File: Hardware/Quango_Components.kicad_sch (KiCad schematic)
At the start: 112 parts, among them J1 Conn_01x12_Male, J2 Conn_01x12_Male, J3 Conn_01x12_Male, J4 Conn_01x12_Male, J5 SWD_Header, J6 Eurorack_10_pin_power, Q1 MMBT3904, U1 LM1117-3.3, U2 STM32G473V, U3 LM1117-5.0, U4 PS508, U5 MCP6002, U6 AS3364, U7 AS3364, U8 AD5676, U9 MCP48CMB21, Y1 8MHz 20pF

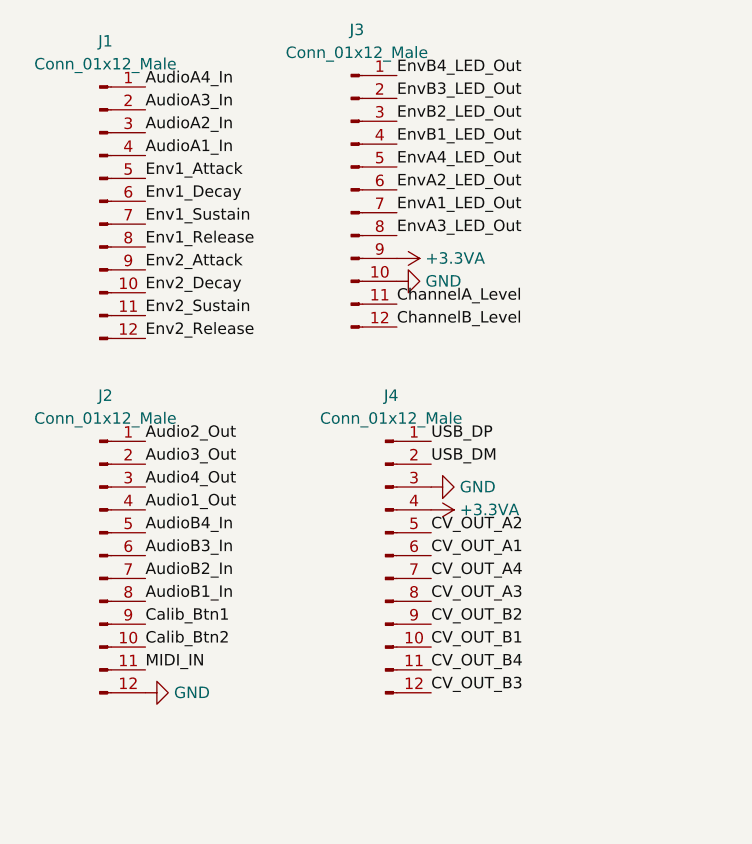
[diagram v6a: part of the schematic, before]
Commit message: Added individual audio channel breakout
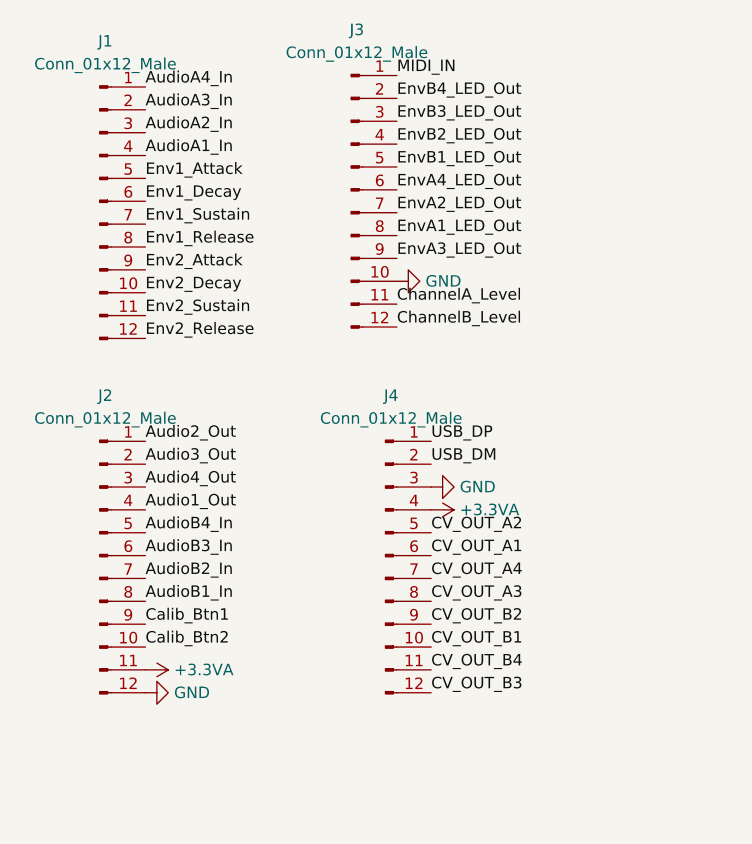
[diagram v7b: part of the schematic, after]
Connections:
- net +3.3VA: now also J2.11 (Pin_11); no longer J3.9 (Pin_9)
- net EnvA1_LED_Out: now also J3.8 (Pin_8); no longer J3.7 (Pin_7)
- net EnvA2_LED_Out: now also J3.7 (Pin_7); no longer J3.6 (Pin_6)
- net EnvA3_LED_Out: now also J3.9 (Pin_9); no longer J3.8 (Pin_8)
- net EnvA4_LED_Out: now also J3.6 (Pin_6); no longer J3.5 (Pin_5)
- net EnvB1_LED_Out: now also J3.5 (Pin_5); no longer J3.4 (Pin_4)
- net EnvB2_LED_Out: now also J3.4 (Pin_4); no longer J3.3 (Pin_3)
- net EnvB3_LED_Out: now also J3.3 (Pin_3); no longer J3.2 (Pin_2)
- net EnvB4_LED_Out: now also J3.2 (Pin_2); no longer J3.1 (Pin_1)
- net MIDI_IN: now also J3.1 (Pin_1); no longer J2.11 (Pin_11)
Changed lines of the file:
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@@
     (effects (font (size 1.27 1.27)) (justify left bottom))
   )
-  (label "EnvA3_LED_Out" (at -175.26 -66.04 0)
+  (label "EnvA3_LED_Out" (at -175.26 -63.5 0)
     (effects (font (size 1.27 1.27)) (justify left bottom))
   )
@@
     (effects (font (size 1.27 1.27)) (justify right bottom))
   )
-  (label "EnvB4_LED_Out" (at -175.26 -83.82 0)
+  (label "EnvB4_LED_Out" (at -175.26 -81.28 0)
     (effects (font (size 1.27 1.27)) (justify left bottom))
   )
@@
     (effects (font (size 1.27 1.27)) (justify left bottom))
   )
-  (label "EnvB2_LED_Out" (at -175.26 -78.74 0)
+  (label "EnvB2_LED_Out" (at -175.26 -76.2 0)
     (effects (font (size 1.27 1.27)) (justify left bottom))
   )
@@
     (effects (font (size 1.27 1.27)) (justify right bottom))
   )
-  (label "MIDI_IN" (at -203.2 -17.78 0)
+  (label "MIDI_IN" (at -175.26 -83.82 0)
     (effects (font (size 1.27 1.27)) (justify left bottom))
   )
@@
     (effects (font (size 1.27 1.27)) (justify left bottom))
   )
-  (label "EnvB3_LED_Out" (at -175.26 -81.28 0)
+  (label "EnvB3_LED_Out" (at -175.26 -78.74 0)
     (effects (font (size 1.27 1.27)) (justify left bottom))
   )
@@
     (effects (font (size 1.27 1.27)) (justify right bottom))
   )
-  (label "EnvA1_LED_Out" (at -175.26 -68.58 0)
+  (label "EnvA1_LED_Out" (at -175.26 -66.04 0)
     (effects (font (size 1.27 1.27)) (justify left bottom))
   )
@@
     (effects (font (size 1.27 1.27)) (justify right bottom))
   )
-  (label "EnvB1_LED_Out" (at -175.26 -76.2 0)
+  (label "EnvB1_LED_Out" (at -175.26 -73.66 0)
     (effects (font (size 1.27 1.27)) (justify left bottom))
   )
@@
     (effects (font (size 1.27 1.27)) (justify right bottom))
   )
-  (label "EnvA4_LED_Out" (at -175.26 -73.66 0)
+  (label "EnvA4_LED_Out" (at -175.26 -71.12 0)
     (effects (font (size 1.27 1.27)) (justify left bottom))
   )
@@
     (effects (font (size 1.27 1.27)) (justify left bottom))
   )
-  (label "EnvA2_LED_Out" (at -175.26 -71.12 0)
+  (label "EnvA2_LED_Out" (at -175.26 -68.58 0)
     (effects (font (size 1.27 1.27)) (justify left bottom))
   )
@@
     (pin "99")
   )
-  (symbol (lib_id "power:+3.3VA") (at -175.26 -63.5 270) (unit 1)
+  (symbol (lib_id "power:+3.3VA") (at -203.2 -17.78 270) (unit 1)
     (in_bom yes) (on_board yes) (fields_autoplaced)
-    (property "Reference" "#PWR02" (id 0) (at -179.07 -63.5 0)
+    (property "Reference" "#PWR02" (id 0) (at -207.01 -17.78 0)
       (effects (font (size 1.27 1.27)) hide)
     )
-    (property "Value" "+3.3VA" (id 1) (at -172.085 -63.5001 90)
+    (property "Value" "+3.3VA" (id 1) (at -200.025 -17.7801 90)
       (effects (font (size 1.27 1.27)) (justify left))
     )
-    (property "Footprint" "" (id 2) (at -175.26 -63.5 0)
+    (property "Footprint" "" (id 2) (at -203.2 -17.78 0)
       (effects (font (size 1.27 1.27)) hide)
     )
-    (property "Datasheet" "" (id 3) (at -175.26 -63.5 0)
+    (property "Datasheet" "" (id 3) (at -203.2 -17.78 0)
       (effects (font (size 1.27 1.27)) hide)
     )
@@
       (reference "J6") (unit 1) (value "Eurorack_10_pin_power") (footprint "Custom_Footprints:Eurorack_10_pin_header")
     )
+    (path "/6505d480-2c4a-43b6-864d-d09e21056980/2e1ddcad-0519-4706-9430-55bb3ce32171"
+      (reference "J7") (unit 1) (value "Audio_Breakout") (footprint "Connector_PinHeader_2.54mm:PinHeader_2x04_P2.54mm_Vertical")
+    )
     (path "/9cc3873a-349e-4fee-be4e-7429042177a8"
       (reference "L1") (unit 1) (value "L_Small") (footprint "Inductor_SMD:L_0805_2012Metric_Pad1.05x1.20mm_HandSolder")
@@
     )
     (path "/6505d480-2c4a-43b6-864d-d09e21056980/1b727df7-cb3f-48d1-be9c-292996b508c3"
-      (reference "U14") (unit 1) (value "TL074") (footprint "Package_SO:TSSOP-14_4.4x5mm_P0.65mm")
+      (reference "U14") (unit 1) (value "TL074") (footprint "Package_SO:SOIC-14_3.9x8.7mm_P1.27mm")
     )
     (path "/6505d480-2c4a-43b6-864d-d09e21056980/dfb0e318-b14d-499c-a2a3-d6ddf83ef63a"
-      (reference "U14") (unit 2) (value "TL074") (footprint "Package_SO:TSSOP-14_4.4x5mm_P0.65mm")
+      (reference "U14") (unit 2) (value "TL074") (footprint "Package_SO:SOIC-14_3.9x8.7mm_P1.27mm")
     )
     (path "/6505d480-2c4a-43b6-864d-d09e21056980/b690f45c-fd5f-4e22-a898-b1a3ca1d64ff"
-      (reference "U14") (unit 3) (value "TL074") (footprint "Package_SO:TSSOP-14_4.4x5mm_P0.65mm")
+      (reference "U14") (unit 3) (value "TL074") (footprint "Package_SO:SOIC-14_3.9x8.7mm_P1.27mm")
     )
     (path "/6505d480-2c4a-43b6-864d-d09e21056980/d7490e05-e2b4-473a-9389-d362b2a1506b"
-      (reference "U14") (unit 4) (value "TL074") (footprint "Package_SO:TSSOP-14_4.4x5mm_P0.65mm")
+      (reference "U14") (unit 4) (value "TL074") (footprint "Package_SO:SOIC-14_3.9x8.7mm_P1.27mm")
     )
     (path "/6505d480-2c4a-43b6-864d-d09e21056980/9b9b9766-bc41-4a1e-b4e6-58c18cc0519f"
-      (reference "U14") (unit 5) (value "TL074") (footprint "Package_SO:TSSOP-14_4.4x5mm_P0.65mm")
+      (reference "U14") (unit 5) (value "TL074") (footprint "Package_SO:SOIC-14_3.9x8.7mm_P1.27mm")
     )
     (path "/226694b0-ec80-4137-9308-0689e83ebb68"

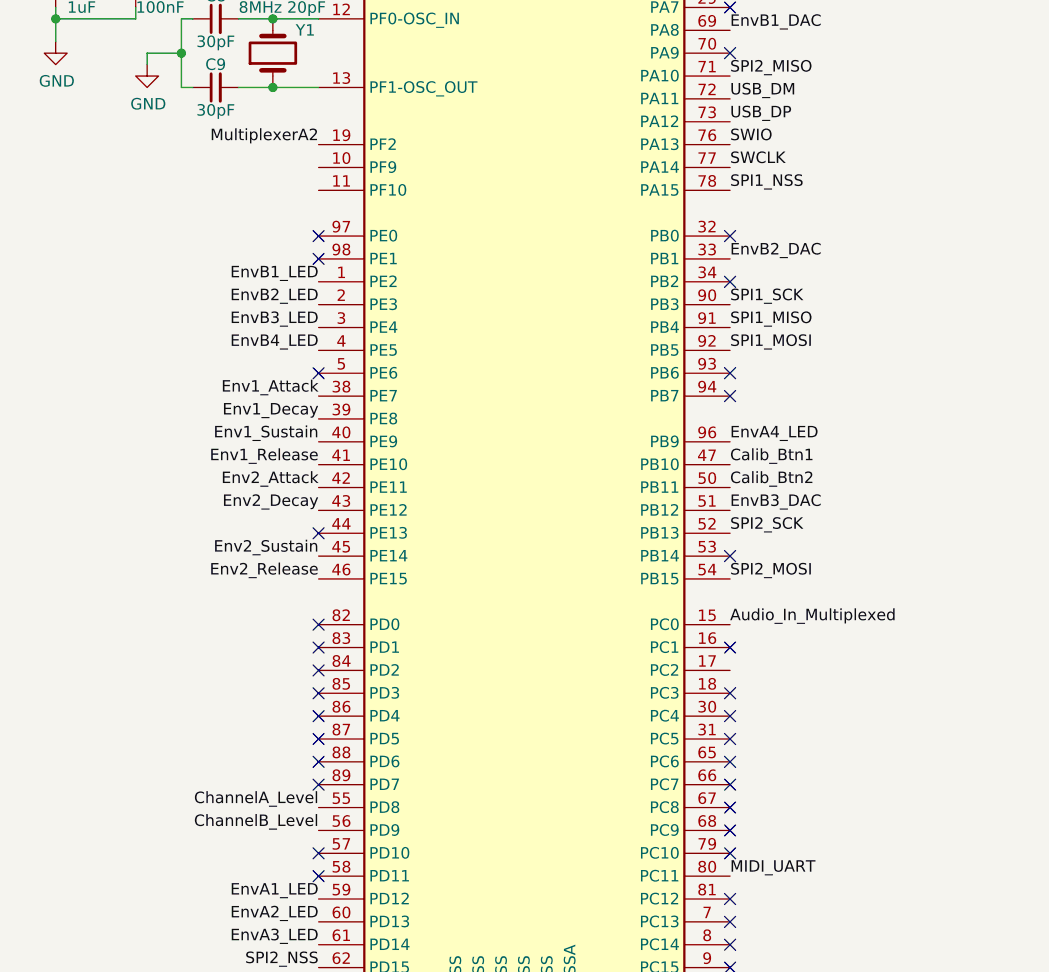
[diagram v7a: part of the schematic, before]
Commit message: Routing Power traces
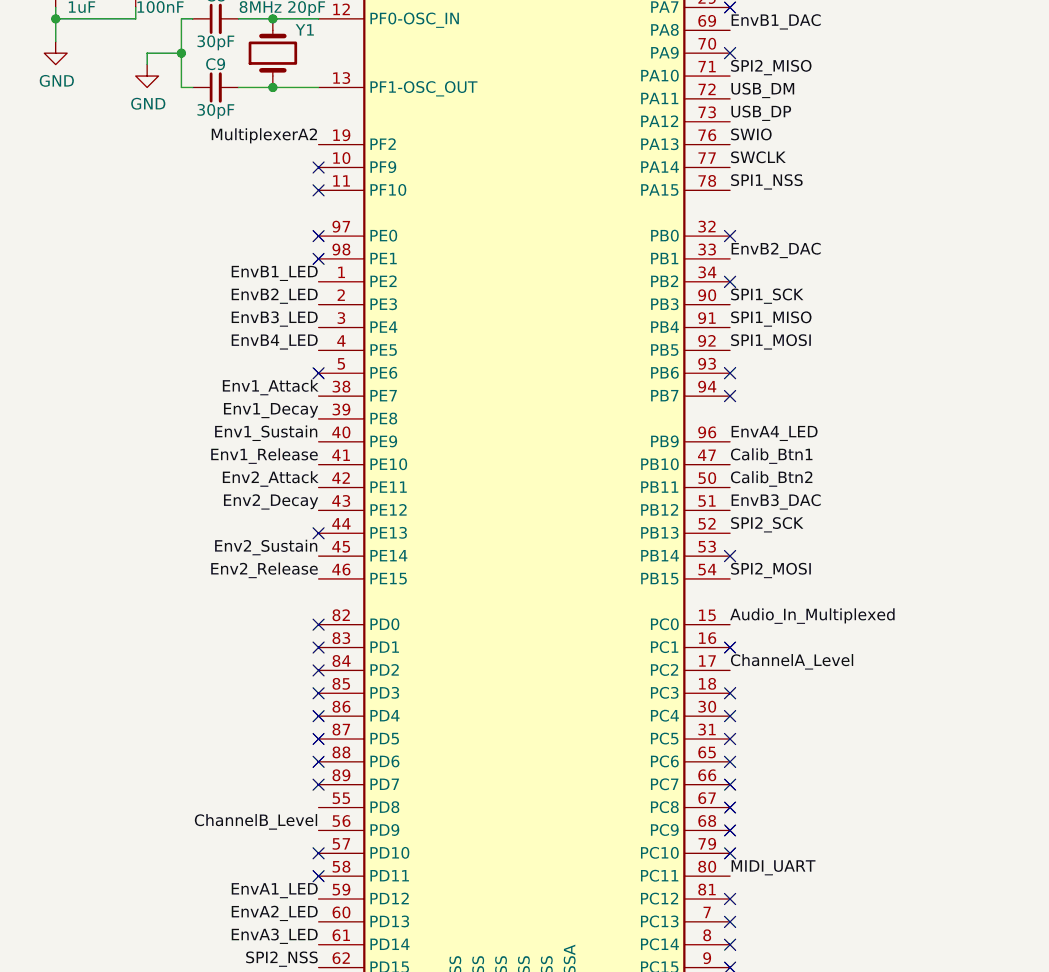
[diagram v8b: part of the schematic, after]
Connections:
- net ChannelA_Level: now also U2.17 (PC2); no longer U2.55 (PD8)
- no-connect marks 35 -> 37
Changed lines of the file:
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@@
   (no_connect (at 53.34 154.94))
   (no_connect (at 99.06 142.24))
+  (no_connect (at 53.34 78.74))
   (no_connect (at 53.34 137.16))
   (no_connect (at 99.06 154.94))
@@
   (no_connect (at 99.06 139.7))
   (no_connect (at 53.34 101.6))
+  (no_connect (at 53.34 81.28))
   (no_connect (at 99.06 160.02))
   (no_connect (at 99.06 91.44))
@@
     (effects (font (size 1.27 1.27)) (justify left bottom))
   )
-  (label "ChannelA_Level" (at 53.34 149.86 180)
-    (effects (font (size 1.27 1.27)) (justify right bottom))
+  (label "ChannelA_Level" (at 99.06 134.62 0)
+    (effects (font (size 1.27 1.27)) (justify left bottom))
   )
   (label "AudioA2_In" (at -203.2 -77.47 0)
@@
     )
     (path "/6505d480-2c4a-43b6-864d-d09e21056980/1b727df7-cb3f-48d1-be9c-292996b508c3"
-      (reference "U14") (unit 1) (value "TL074") (footprint "Package_SO:SOIC-14_3.9x8.7mm_P1.27mm")
+      (reference "U14") (unit 1) (value "TL074") (footprint "Package_SO:TSSOP-14_4.4x5mm_P0.65mm")
     )
     (path "/6505d480-2c4a-43b6-864d-d09e21056980/dfb0e318-b14d-499c-a2a3-d6ddf83ef63a"
-      (reference "U14") (unit 2) (value "TL074") (footprint "Package_SO:SOIC-14_3.9x8.7mm_P1.27mm")
+      (reference "U14") (unit 2) (value "TL074") (footprint "Package_SO:TSSOP-14_4.4x5mm_P0.65mm")
     )
     (path "/6505d480-2c4a-43b6-864d-d09e21056980/b690f45c-fd5f-4e22-a898-b1a3ca1d64ff"
-      (reference "U14") (unit 3) (value "TL074") (footprint "Package_SO:SOIC-14_3.9x8.7mm_P1.27mm")
+      (reference "U14") (unit 3) (value "TL074") (footprint "Package_SO:TSSOP-14_4.4x5mm_P0.65mm")
     )
     (path "/6505d480-2c4a-43b6-864d-d09e21056980/d7490e05-e2b4-473a-9389-d362b2a1506b"
-      (reference "U14") (unit 4) (value "TL074") (footprint "Package_SO:SOIC-14_3.9x8.7mm_P1.27mm")
+      (reference "U14") (unit 4) (value "TL074") (footprint "Package_SO:TSSOP-14_4.4x5mm_P0.65mm")
     )
     (path "/6505d480-2c4a-43b6-864d-d09e21056980/9b9b9766-bc41-4a1e-b4e6-58c18cc0519f"
-      (reference "U14") (unit 5) (value "TL074") (footprint "Package_SO:SOIC-14_3.9x8.7mm_P1.27mm")
+      (reference "U14") (unit 5) (value "TL074") (footprint "Package_SO:TSSOP-14_4.4x5mm_P0.65mm")
     )
     (path "/226694b0-ec80-4137-9308-0689e83ebb68"
